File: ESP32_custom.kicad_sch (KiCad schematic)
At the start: 28 parts, among them J1 TYPE-C-31-M-12, J2 Conn_01x16_Pin, J3 Conn_01x16_Pin, Q1 SS8050, Q2 SS8050, SW1 SW_Push, SW2 SW_Push, U2 ESP32-WROOM-32E 8MB, U3 CH340C, U4 AMS1117-3.3

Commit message: define stackup (non-precise calculation
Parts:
- R11, R12: footprint (none) -> Resistor_SMD:R_0402_1005Metric
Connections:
- net +5V: no longer J2.1 (Pin_1)
- net VCC: now also J2.1 (Pin_1)
- net D11 renamed D-
- net D22 renamed D+
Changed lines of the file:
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@@
 		)
 	)
-	(label "D11"
+	(label "D-"
 		(at 41.91 60.96 180)
 		(effects
@@
 		)
 	)
-	(label "D22"
+	(label "D+"
 		(at 41.91 58.42 180)
 		(effects
@@
 		)
 	)
-	(label "D22"
+	(label "D+"
 		(at 74.93 142.24 0)
 		(effects
@@
 		)
 	)
-	(label "D11"
+	(label "D-"
 		(at 68.58 144.78 180)
 		(effects
@@
 	)
 	(symbol
-		(lib_id "power:+5V")
-		(at 201.93 38.1 0)
-		(unit 1)
-		(body_style 1)
-		(exclude_from_sim no)
-		(in_bom yes)
-		(on_board yes)
-		(in_pos_files yes)
-		(dnp no)
-		(fields_autoplaced yes)
-		(property "Reference" "#PWR016"
-			(at 201.93 41.91 0)
-			(hide yes)
-			(show_name no)
-			(do_not_autoplace no)
-			(effects
-				(font
-					(size 1.27 1.27)
-				)
-			)
-		)
-		(property "Value" "+5V"
-			(at 201.93 33.02 0)
-			(show_name no)
-			(do_not_autoplace no)
-			(effects
-				(font
-					(size 1.27 1.27)
-				)
-			)
-		)
-		(property "Footprint" ""
-			(at 201.93 38.1 0)
-			(hide yes)
-			(show_name no)
-			(do_not_autoplace no)
-			(effects
-				(font
-					(size 1.27 1.27)
-				)
-			)
-		)
-		(property "Datasheet" ""
-			(at 201.93 38.1 0)
-			(hide yes)
-			(show_name no)
-			(do_not_autoplace no)
-			(effects
-				(font
-					(size 1.27 1.27)
-				)
-			)
-		)
-		(property "Description" "Power symbol creates a global label with name \"+5V\""
-			(at 201.93 38.1 0)
-			(hide yes)
-			(show_name no)
-			(do_not_autoplace no)
-			(effects
-				(font
-					(size 1.27 1.27)
-				)
-			)
-		)
-		(pin "1"
-		)
-		(instances
-			(project "ESP32_custom"
-				(path "/d69a2644-c978-49ae-b7c7-18eba523ada2"
-					(reference "#PWR016")
-					(unit 1)
-				)
-			)
-		)
-	)
-	(symbol
 		(lib_id "Device:C")
 		(at 69.85 106.68 90)
@@
 			)
 		)
-		(property "Footprint" ""
+		(property "Footprint" "Resistor_SMD:R_0402_1005Metric"
 			(at 24.892 171.45 90)
 			(hide yes)
@@
 			)
 		)
-		(property "Footprint" ""
+		(property "Footprint" "Resistor_SMD:R_0402_1005Metric"
 			(at 80.772 171.45 90)
 			(hide yes)
@@
 					(unit 1)
 				)
+			)
+		)
+	)
+	(symbol
+		(lib_id "power:VCC")
+		(at 201.93 38.1 0)
+		(unit 1)
+		(body_style 1)
+		(exclude_from_sim no)
+		(in_bom yes)
+		(on_board yes)
+		(in_pos_files yes)
+		(dnp no)
+		(fields_autoplaced yes)
+		(property "Reference" "#PWR012"
+			(at 201.93 41.91 0)
+			(hide yes)
+			(show_name no)
+			(do_not_autoplace no)
+			(effects
+				(font
+					(size 1.27 1.27)
+				)
+			)
+		)
+		(property "Value" "VCC"
+			(at 201.93 33.02 0)
+			(show_name no)
+			(do_not_autoplace no)
+			(effects
+				(font
+					(size 1.27 1.27)
+				)
+			)
+		)
+		(property "Footprint" ""
+			(at 201.93 38.1 0)
+			(hide yes)
+			(show_name no)
+			(do_not_autoplace no)
+			(effects
+				(font
+					(size 1.27 1.27)
+				)
+			)
+		)
+		(property "Datasheet" ""
+			(at 201.93 38.1 0)
+			(hide yes)
+			(show_name no)
+			(do_not_autoplace no)
+			(effects
+				(font
+					(size 1.27 1.27)
+				)
+			)
+		)
+		(property "Description" "Power symbol creates a global label with name \"VCC\""
+			(at 201.93 38.1 0)
+			(hide yes)
+			(show_name no)
+			(do_not_autoplace no)
+			(effects
+				(font
+					(size 1.27 1.27)
+				)
+			)
+		)
+		(pin "1"
+		)
+		(instances
+			(project "ESP32_custom"
+				(path "/d69a2644-c978-49ae-b7c7-18eba523ada2"
+					(reference "#PWR012")
+					(unit 1)
+				)

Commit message: routing DRC fail
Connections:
- net RX: now also R2.2; no longer R1.2
- net TX: now also R1.2; no longer R2.2
- net CC1: now reaches J1.A5 (CC1), R12.1
- net CC2: now reaches J1.B5 (CC2), R11.1
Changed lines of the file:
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@@
 		)
 	)
-	(label "TX"
+	(label "RX"
 		(at 76.2 48.26 0)
 		(effects
@@
 		)
 	)
-	(label "RX"
+	(label "TX"
 		(at 76.2 55.88 0)
 		(effects
@@
 		)
 	)
+	(label "CC1"
+		(at 33.02 158.75 0)
+		(effects
+			(font
+				(size 1.27 1.27)
+			)
+			(justify left bottom)
+		)
+	)
 	(label "IO14"
 		(at 198.12 67.31 0)
@@
 		(effects
 			(font
+				(size 1.27 1.27)
+			)
+			(justify left bottom)
+		)
+	)
+	(label "CC2"
+		(at 73.66 166.37 0)
+		(effects
+			(font

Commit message: update schematic (reduced pin header)
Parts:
- removed J2, J3: Conn_01x16_Pin, Connector_PinHeader_2.54mm:PinHeader_1x16_P2.54mm_Vertical, symbol Connector:Conn_01x16_Pin
- added J2, J3: Conn_01x13_Pin, symbol Connector:Conn_01x13_Pin
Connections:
- net +5V: now also J2.13 (Pin_13)
- net EN: now also J2.2 (Pin_2)
- net GND: now also J2.12 (Pin_12), J3.1 (Pin_1)
- net IO13: now also J2.11 (Pin_11)
- net IO14: now also J2.10 (Pin_10)
- net IO15: now also J3.13 (Pin_13)
- net IO16: now also J3.11 (Pin_11)
- net IO17: now also J3.10 (Pin_10)
- net IO18: now also J3.8 (Pin_8)
- net IO19: now also J3.7 (Pin_7)
- net IO21: now also J3.6 (Pin_6)
- net IO22: now also J3.3 (Pin_3)
- net IO23: now also J3.2 (Pin_2)
- net IO25: now also J2.7 (Pin_7)
- net IO26: now also J2.8 (Pin_8)
- net IO27: now also J2.9 (Pin_9)
- net IO32: now also J2.5 (Pin_5)
- net IO33: now also J2.6 (Pin_6)
- net IO4: now also J3.12 (Pin_12)
- net IO5: now also J3.9 (Pin_9)
- net RX: now also J3.4 (Pin_4)
- net TX: now also J3.5 (Pin_5)
- net VCC: now also J2.1 (Pin_1)
- net VN: now also J2.4 (Pin_4)
- net VP: now also J2.3 (Pin_3)

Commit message: finish routing (DRC fail)
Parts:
- J2, J3: footprint (none) -> Connector_PinHeader_2.54mm:PinHeader_1x13_P2.54mm_Vertical
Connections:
- net IO12: no longer names the net of U2.14 (IO12)
- net IO34: no longer names the net of U2.6 (IO34)
- net IO35: no longer names the net of U2.7 (IO35)
- no-connect marks 8 -> 10
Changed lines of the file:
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@@
 	)
 	(no_connect
+		(at 110.49 62.23)
+	)
+	(no_connect
 		(at 62.23 63.5)
 	)
 	(no_connect
+		(at 110.49 59.69)
+	)
+	(no_connect
 		(at 71.12 171.45)
 	)
@@
 		)
 	)
-	(label "IO35"
-		(at 110.49 62.23 180)
-		(effects
-			(font
-				(size 1.27 1.27)
-			)
-			(justify right bottom)
-		)
-	)
 	(label "IO19"
 		(at 215.9 50.8 0)
@@
 		)
 	)
-	(label "IO34"
-		(at 110.49 59.69 180)
-		(effects
-			(font
-				(size 1.27 1.27)
-			)
-			(justify right bottom)
-		)
-	)
 	(label "IO26"
 		(at 190.5 53.34 0)
@@
 		)
 	)
-	(label "IO12"
-		(at 110.49 80.01 180)
-		(effects
-			(font
-				(size 1.27 1.27)
-			)
-			(justify right bottom)
-		)
-	)
 	(label "IO25"
 		(at 110.49 69.85 180)
@@
 			)
 		)
-		(property "Footprint" ""
+		(property "Footprint" "Connector_PinHeader_2.54mm:PinHeader_1x13_P2.54mm_Vertical"
 			(at 210.82 50.8 0)
 			(hide yes)
@@
 			)
 		)
-		(property "Footprint" ""
+		(property "Footprint" "Connector_PinHeader_2.54mm:PinHeader_1x13_P2.54mm_Vertical"
 			(at 185.42 50.8 0)
 			(hide yes)

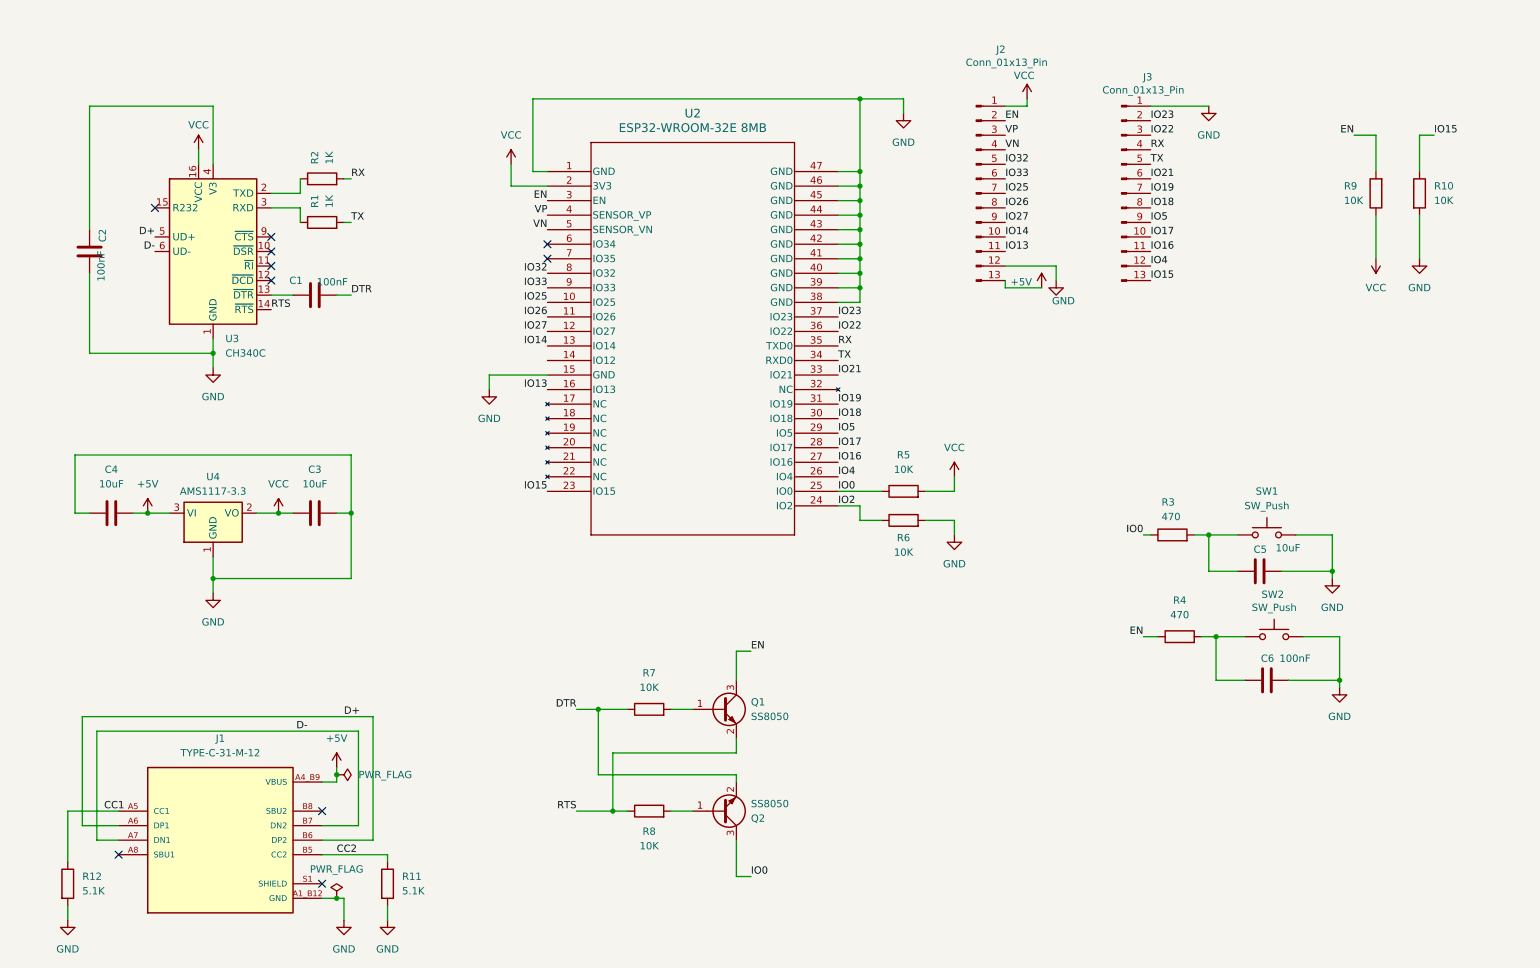
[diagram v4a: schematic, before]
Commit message: update schematic. changed to esp32-s3
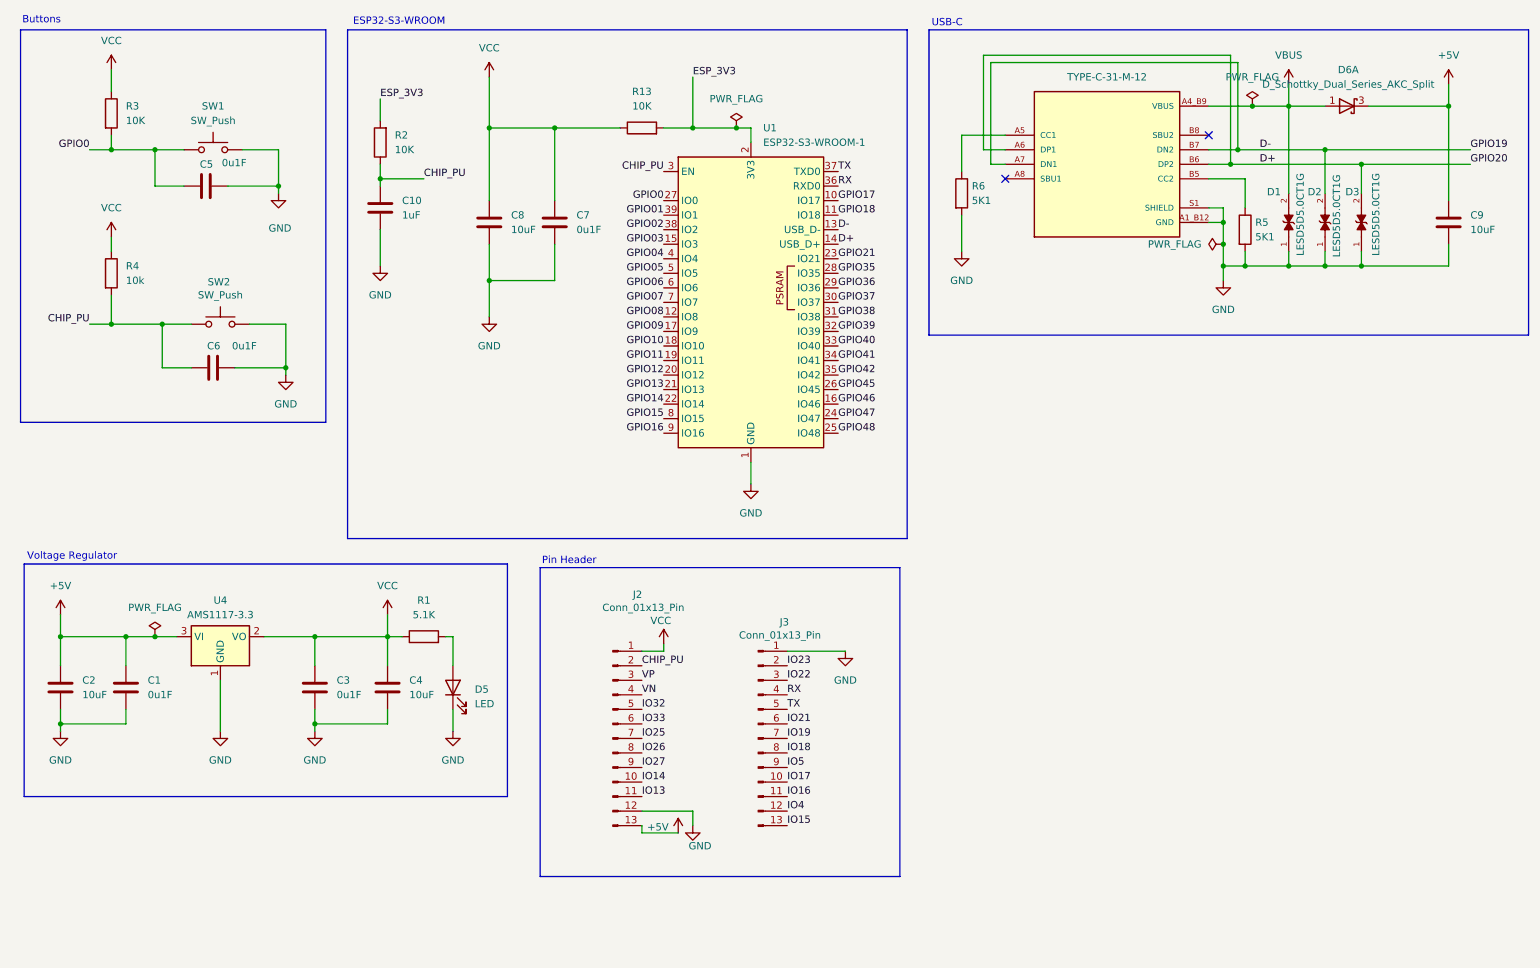
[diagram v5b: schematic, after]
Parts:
- removed Q1, Q2: SS8050, Package_TO_SOT_SMD:SOT-23-3, symbol Transistor_BJT:SS8050
- removed R10, R7, R8, R9: 10K, Resistor_SMD:R_0402_1005Metric, symbol Device:R
- removed R11, R12: 5.1K, Resistor_SMD:R_0402_1005Metric, symbol Device:R
- removed U2: ESP32-WROOM-32E 8MB, KiCADv6:ESP32­WROOM­32E_EXP, symbol 2026-08-21_16-20-42:ESP32-WROOM-32E_8MB
- removed U3: CH340C, Package_SO:SOIC-16_3.9x9.9mm_P1.27mm, symbol Interface_USB:CH340C
- added C10: 1uF, symbol Device:C
- added C7: 0u1F, symbol Device:C
- added C8, C9: 10uF, symbol Device:C
- added D1, D2, D3: LESD5D5.0CT1G, LESD5D5.0CT1G:TVS_LESD5D5.0CT1G, symbol LESD5D5.0CT1G:LESD5D5.0CT1G
- added D5: LED, symbol Device:LED
- added D6: D_Schottky_Dual_Series_AKC_Split, Button_Switch_SMD:SW_DIP_SPSTx01_Slide_Copal_CVS-01xB_W5.9mm_P1mm, symbol Device:D_Schottky_Dual_Series_AKC_Split
- added R13: 10K, symbol Device:R
- added U1: ESP32-S3-WROOM-1, RF_Module:ESP32-S3-WROOM-1, symbol RF_Module:ESP32-S3-WROOM-1
- C1: value 100nF -> 0u1F; footprint Capacitor_SMD:C_0402_1005Metric -> (none)
- C2: value 100nF -> 10uF; footprint Capacitor_SMD:C_0402_1005Metric -> (none)
- C3: value 10uF -> 0u1F; footprint Capacitor_SMD:C_0402_1005Metric -> (none)
- C4: footprint Capacitor_SMD:C_0402_1005Metric -> (none)
- C5: value 10uF -> 0u1F
- C6: value 100nF -> 0u1F
- R1: value 1K -> 5.1K; footprint Resistor_SMD:R_0402_1005Metric -> (none)
- R2: value 1K -> 10K; footprint Resistor_SMD:R_0402_1005Metric -> (none)
- R3: value 470 -> 10K; footprint Resistor_SMD:R_0402_1005Metric -> (none)
- R4: value 470 -> 10k; footprint Resistor_SMD:R_0402_1005Metric -> (none)
- R5, R6: value 10K -> 5K1; footprint Resistor_SMD:R_0402_1005Metric -> (none)
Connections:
- net DTR is gone; now on net GND: C1.2
- net IO2 is gone; now on an unnamed net: R6.1
- net +5V: now also C1.1, C2.1, C9.1, D6.3 (K); no longer C4.2, J1.A4_B9 (VBUS), J1.B4_A9 (VBUS)
- net D+: now also D3.2, U1.14 (USB_D+)
- net D-: now also D2.2, U1.13 (USB_D-)
- net GND: now also C4.2, J1.S1 (SHIELD), J1.S2 (SHIELD), J1.S3 (SHIELD), J1.S4 (SHIELD), R5.2, C10.2, C7.2, C8.2, C9.2, D1.1, D2.1, D3.1, D5.1 (K), U1.1 (GND), U1.40 (GND), U1.41 (GND); no longer C4.1
- net RX: now also U1.36 (RXD0); no longer R2.2
- net TX: now also U1.37 (TXD0); no longer R1.2
- net VCC: now also C4.1, R1.1, R3.1, R4.1, C7.1, C8.1, R13.1; no longer R5.2
- net CHIP_PU: now reaches R2.1
- net CHIP_PU: now also C6.1, J2.2 (Pin_2), R4.2, SW2.1, C10.1, U1.3 (EN)
- net GPIO0: now reaches C5.1, R3.2, SW1.1
- net GPIO0: now also U1.27 (IO0)
- net CC1: no longer names the net of J1.A5 (CC1)
- net CC2: no longer names the net of J1.B5 (CC2)
- net CC2: now also R5.1
- removed net EN: J2.2 (Pin_2), R4.1
- removed net IO0: R3.1, R5.1
- new net: D5.2 (A), R1.2
- new net ESP_3V3: R13.2, R2.2, U1.2 (3V3)
- new net GPIO01: U1.39 (IO1)
- new net GPIO02: U1.38 (IO2)
- new net GPIO03: U1.15 (IO3)
- new net GPIO04: U1.4 (IO4)
- new net GPIO05: U1.5 (IO5)
- new net GPIO06: U1.6 (IO6)
- new net GPIO07: U1.7 (IO7)
- new net GPIO08: U1.12 (IO8)
- new net GPIO09: U1.17 (IO9)
- new net GPIO10: U1.18 (IO10)
- new net GPIO11: U1.19 (IO11)
- new net GPIO12: U1.20 (IO12)
- new net GPIO13: U1.21 (IO13)
- new net GPIO14: U1.22 (IO14)
- new net GPIO15: U1.8 (IO15)
- new net GPIO16: U1.9 (IO16)
- new net GPIO17: U1.10 (IO17)
- new net GPIO18: U1.11 (IO18)
- new net GPIO21: U1.23 (IO21)
- new net GPIO35: U1.28 (IO35)
- new net GPIO36: U1.29 (IO36)
- new net GPIO37: U1.30 (IO37)
- new net GPIO38: U1.31 (IO38)
- new net GPIO39: U1.32 (IO39)
- new net GPIO40: U1.33 (IO40)
- new net GPIO41: U1.34 (IO41)
- new net GPIO42: U1.35 (IO42)
- new net GPIO45: U1.26 (IO45)
- new net GPIO46: U1.16 (IO46)
- new net GPIO47: U1.24 (IO47)
- new net GPIO48: U1.25 (IO48)
- new net VBUS: D1.2, D6.1 (A), J1.A4_B9 (VBUS), J1.B4_A9 (VBUS)
- no-connect marks 10 -> 2
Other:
- note added: "Buttons"
- note added: "ESP32-S3-WROOM"
- note added: "Pin Header"
- note added: "USB-C"
- note added: "Voltage Regulator"
- moved on the sheet: C5, C6, J2, J3, SW1, SW2, U4

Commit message: assign footprint
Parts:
- C1, C10, C2, C3, C4, C7, C8, C9: footprint (none) -> Capacitor_SMD:C_0402_1005Metric
- D5: footprint (none) -> LED_SMD:LED_0201_0603Metric
- D6: footprint Button_Switch_SMD:SW_DIP_SPSTx01_Slide_Copal_CVS-01xB_W5.9mm_P1mm -> Diode_SMD:D_0201_0603Metric
- R1, R13, R2, R3, R4, R5, R6: footprint (none) -> Resistor_SMD:R_0201_0603Metric
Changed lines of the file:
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@@
 			)
 		)
-		(property "Footprint" ""
+		(property "Footprint" "Capacitor_SMD:C_0402_1005Metric"
 			(at 37.7952 140.97 0)
 			(hide yes)
@@
 			)
 		)
-		(property "Footprint" ""
+		(property "Footprint" "Capacitor_SMD:C_0402_1005Metric"
 			(at 112.7252 59.69 0)
 			(hide yes)
@@
 			)
 		)
-		(property "Footprint" ""
+		(property "Footprint" "Capacitor_SMD:C_0402_1005Metric"
 			(at 83.5152 140.97 0)
 			(hide yes)
@@
 			)
 		)
-		(property "Footprint" ""
+		(property "Footprint" "Capacitor_SMD:C_0402_1005Metric"
 			(at 26.3652 140.97 0)
 			(hide yes)
@@
 			)
 		)
-		(property "Footprint" ""
+		(property "Footprint" "Resistor_SMD:R_0201_0603Metric"
 			(at 127 41.148 90)
 			(hide yes)
@@
 			)
 		)
-		(property "Footprint" ""
+		(property "Footprint" "Capacitor_SMD:C_0402_1005Metric"
 			(at 268.9352 59.69 0)
 			(hide yes)
@@
 			)
 		)
-		(property "Footprint" ""
+		(property "Footprint" "Resistor_SMD:R_0201_0603Metric"
 			(at 181.102 50.8 90)
 			(hide yes)
@@
 			)
 		)
-		(property "Footprint" ""
+		(property "Footprint" "Capacitor_SMD:C_0402_1005Metric"
 			(at 70.8152 140.97 0)
 			(hide yes)
@@
 			)
 		)
-		(property "Footprint" ""
+		(property "Footprint" "Capacitor_SMD:C_0402_1005Metric"
 			(at 101.2952 59.69 0)
 			(hide yes)
@@
 			)
 		)
-		(property "Footprint" ""
+		(property "Footprint" "Resistor_SMD:R_0201_0603Metric"
 			(at 32.512 64.77 90)
 			(hide yes)
@@
 			)
 		)
-		(property "Footprint" ""
+		(property "Footprint" "Resistor_SMD:R_0201_0603Metric"
 			(at 88.9 130.048 90)
 			(hide yes)
@@
 			)
 		)
-		(property "Footprint" ""
+		(property "Footprint" "Resistor_SMD:R_0201_0603Metric"
 			(at 230.632 57.15 90)
 			(hide yes)
@@
 			)
 		)
-		(property "Footprint" ""
+		(property "Footprint" "Capacitor_SMD:C_0402_1005Metric"
 			(at 82.2452 57.15 0)
 			(hide yes)
@@
 			)
 		)
-		(property "Footprint" ""
+		(property "Footprint" "LED_SMD:LED_0201_0603Metric"
 			(at 93.98 137.16 0)
 			(hide yes)
@@
 			)
 		)
-		(property "Footprint" "Button_Switch_SMD:SW_DIP_SPSTx01_Slide_Copal_CVS-01xB_W5.9mm_P1mm"
+		(property "Footprint" "Diode_SMD:D_0201_0603Metric"
 			(at 247.65 38.1 0)
 			(hide yes)
@@
 			)
 		)
-		(property "Footprint" ""
+		(property "Footprint" "Resistor_SMD:R_0201_0603Metric"
 			(at 83.058 41.91 90)
 			(hide yes)
@@
 			)
 		)
-		(property "Footprint" ""
+		(property "Footprint" "Resistor_SMD:R_0201_0603Metric"
 			(at 32.512 36.83 90)
 			(hide yes)
